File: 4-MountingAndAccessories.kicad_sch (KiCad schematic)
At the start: 16 parts, among them J401 Spring Contact

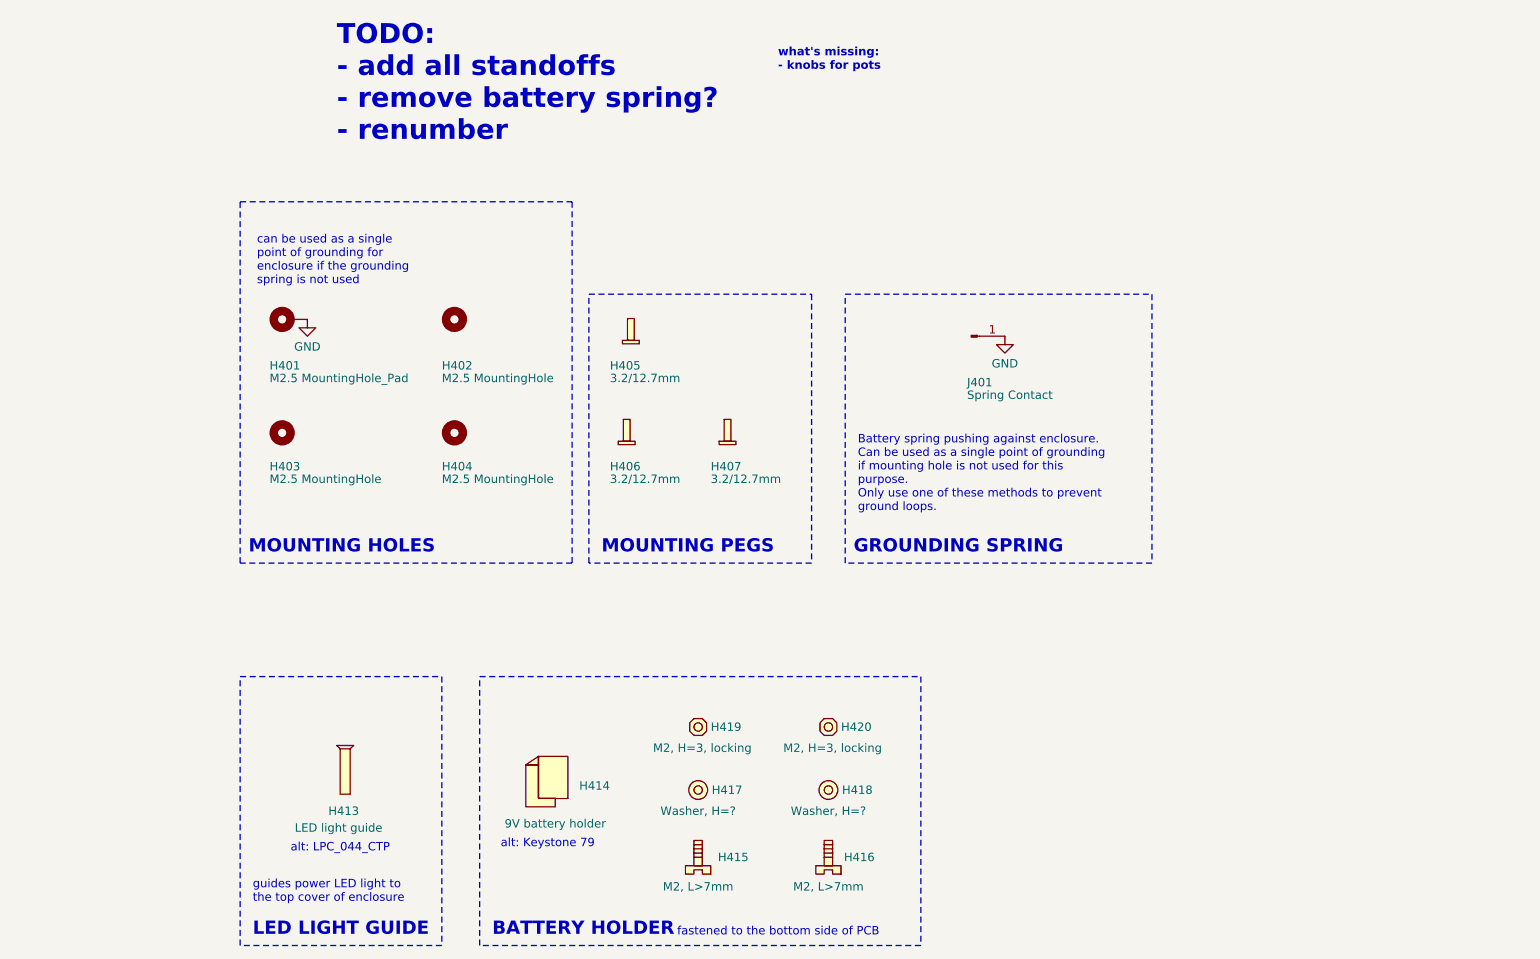
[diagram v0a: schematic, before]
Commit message: schematic: finishing standoffs, screws, minor improvements
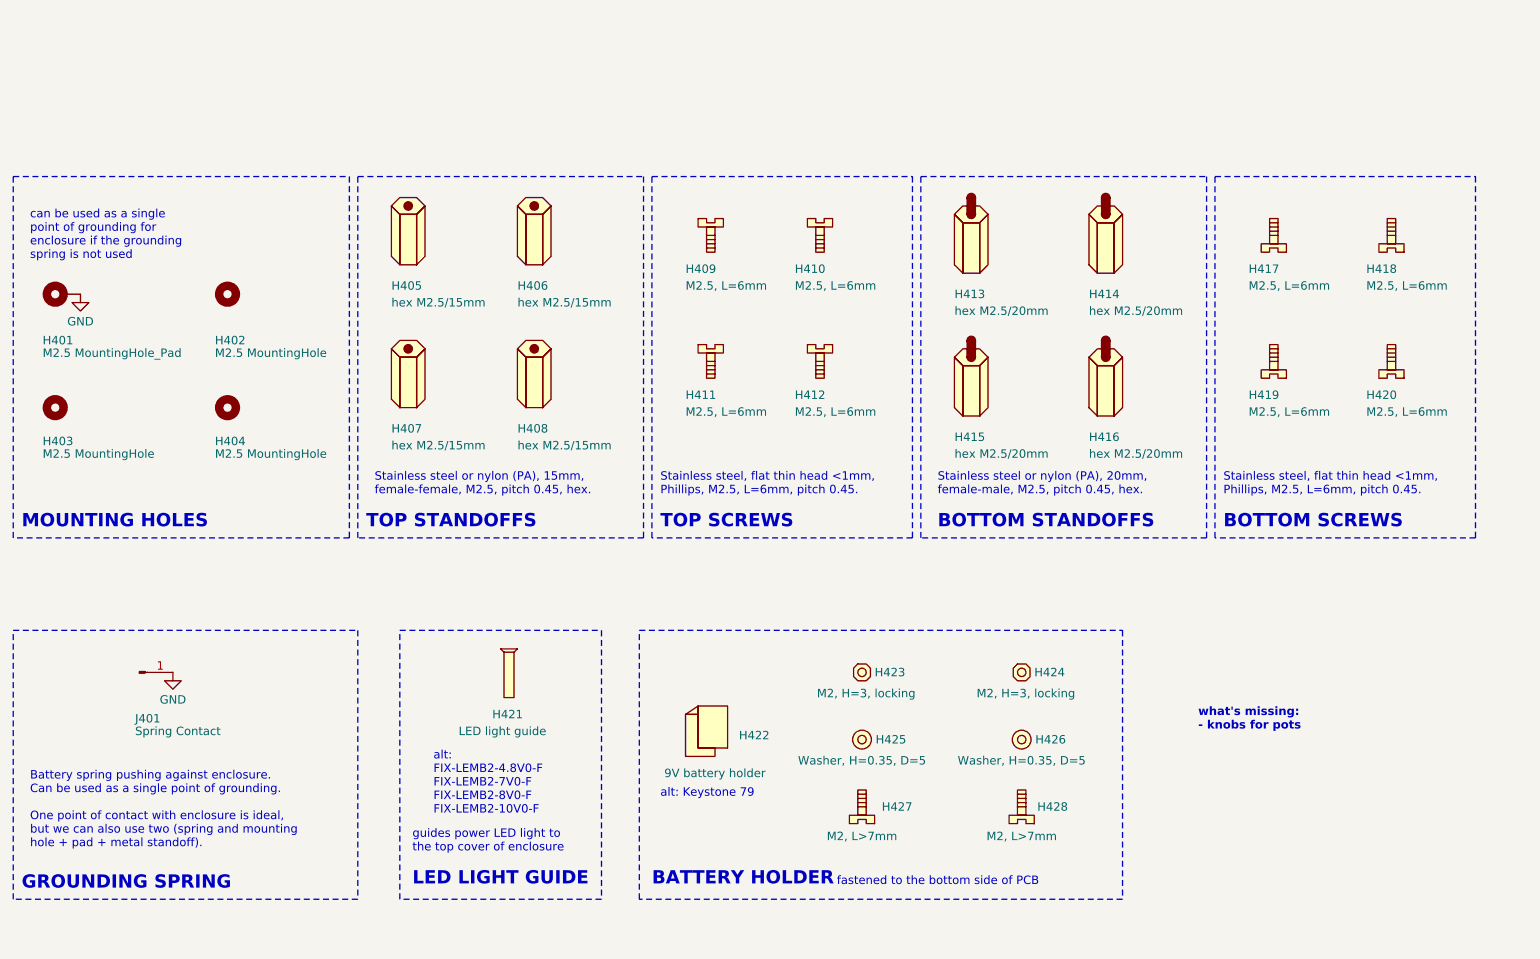
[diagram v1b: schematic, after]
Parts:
- removed H405, H406, H407: 3.2/12.7mm, symbol MountingPegs:MountingPeg
- removed H418: Washer, H=?, symbol Washer:Washer
- added H405, H406, H407, H408: hex M2.5/15mm, symbol StandoffPCB:Standoff_Female_Female
- added H409, H410, H411, H412, H417, H418, H419, H420: M2.5, L=6mm, symbol Bolt:Bolt
- added H413, H414, H415, H416: hex M2.5/20mm, symbol StandoffPCB:Standoff_Female_Male
- added H426: Washer, H=0.35, D=5, symbol Washer:Washer
- H401, H402, H403, H404: now left out of the parts list
- H421: renamed from H413; Mfr Part # PLPC3-10MM -> FIX-LEMB2-10V0-F; Mouser Part # 749-PLPC310MM -> -; Purpose LED light pipe from top of the enclosure to LED -> LED light pipe from top of the enclosure to LED. Dia guide 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; Source Mouser -> TME; TME Part # PLPC3-10MM -> FIX-LEMB2-10V0-F
- H423: renamed from H419; LCSC Part # (none) -> -; Mfr (none) -> -; Mfr Part # (none) -> -; Mouser Part # (none) -> -; TME Part # (none) -> -
- H425: renamed from H417; value Washer, H=? -> Washer, H=0.35, D=5; LCSC Part # (none) -> -; Mfr (none) -> -; Mfr Part # (none) -> -; Mouser Part # (none) -> -; TME Part # (none) -> -
- H427: renamed from H415; LCSC Part # (none) -> -; Mfr (none) -> -; Mfr Part # (none) -> -; Mouser Part # (none) -> -; TME Part # (none) -> -
- H428: renamed from H416; LCSC Part # (none) -> -; Mfr (none) -> -; Mfr Part # (none) -> -; Mouser Part # (none) -> -; Source (none) -> -; TME Part # (none) -> -
- J401: Source TME -> Mouser
- renumbered H414 to H422, H420 to H424
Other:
- note added: "BOTTOM SCREWS"
- note added: "BOTTOM STANDOFFS"
- note added: "Battery spring pushing against enclosure. Can be used as a single point of grounding. One point of contact with enclosure is ideal, but we can also use two (spring and mounting hole + pad + metal standoff)."
- note added: "Stainless steel or nylon (PA), 15mm, female-female, M2.5, pitch 0.45, hex."
- note added: "Stainless steel or nylon (PA), 20mm, female-male, M2.5, pitch 0.45, hex."
- note added: "Stainless steel, flat thin head <1mm, Phillips, M2.5, L=6mm, pitch 0.45."
- note added: "TOP SCREWS"
- note added: "TOP STANDOFFS"
- note added: "alt: FIX-LEMB2-4.8V0-F FIX-LEMB2-7V0-F FIX-LEMB2-8V0-F FIX-LEMB2-10V0-F"
- note removed: "Battery spring pushing against enclosure. Can be used as a single point of grounding if mounting hole is not used for this purpose. Only use one of these methods to prevent ground loops."
- note removed: "MOUNTING PEGS"
- note removed: "TODO: - add all standoffs - remove battery spring? - renumber"
- note removed: "alt: LPC_044_CTP"
- moved on the sheet: H401, H402, H403, H404, H421, H422, H423, H424, H425, H427, H428, J401

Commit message: Schematic, PCB: moving DC ESD protection in front of the switch. Using one 22uF bulk decoupling cap where DC enters the board instead of two 10uF near opamps. Using 22uF instead of 10uF in opamp biasing to remove 10uF from BOM completely
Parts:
- H422: Mfr Part # 71 -> 79; Mouser Part # 534-071 -> 534-079; TME Part # KEYS71 -> KEYS79
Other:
- note added: "alt: Keystone 71 (bit too short)"
- note removed: "alt: Keystone 79"
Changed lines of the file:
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@@
 	(title_block
 		(title "Mounting, hardware and accessories")
-		(date "2024-02-20")
+		(date "2024-03-07")
 		(rev "3.0")
 		(company "Arx")
@@
 		)
 	)
-	(text "alt: Keystone 79"
-		(exclude_from_sim no)
-		(at 139.7 119.38 0)
+	(text "alt: Keystone 71\n(bit too short)"
+		(exclude_from_sim no)
+		(at 139.7 121.92 0)
 		(effects
 			(font
@@
 			)
 		)
-		(property "Datasheet" "https://cz.mouser.com/datasheet/2/215/1-745942.pdf"
+		(property "Datasheet" "https://cz.mouser.com/datasheet/2/215/9-745395.pdf"
 			(at 146.05 108.585 0)
 			(effects
@@
 			)
 		)
-		(property "Mfr Part #" "71"
+		(property "Mfr Part #" "79"
 			(at 146.05 108.585 0)
 			(effects
@@
 			)
 		)
-		(property "Mouser Part #" "534-071"
+		(property "Mouser Part #" "534-079"
 			(at 146.05 108.585 0)
 			(effects
@@
 			)
 		)
-		(property "TME Part #" "KEYS71"
+		(property "TME Part #" "KEYS79"
 			(at 146.05 108.585 0)
 			(effects

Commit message: schematic: optimizing few BOM items (for less costly alternatives), few updates
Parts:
- H421: Alt (none) -> FIX-LEMB2-4.8V0-F, FIX-LEMB2-7V0-F, FIX-LEMB2-8V0-F, FIX-LE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
- H422: Alt (none) -> 71 (too short)
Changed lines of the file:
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@@
 	(title_block
 		(title "Mounting, hardware and accessories")
-		(date "2024-03-07")
+		(date "2024-03-10")
 		(rev "3.0")
 		(company "Arx")
@@
 			)
 		)
+		(property "Alt" "71 (too short)"
+			(at 146.05 108.585 0)
+			(effects
+				(font
+					(size 1.27 1.27)
+				)
+				(hide yes)
+			)
+		)
 		(instances
 			(project "2024_PiezoPreamp3"
@@
 			(at 116.84 100.33 0)
 			(effects
+				(font
+					(size 1.27 1.27)
+				)
+				(hide yes)
+			)
+		)
+		(property "Alt" "FIX-LEMB2-4.8V0-F, FIX-LEMB2-7V0-F, FIX-LEMB2-8V0-F, FIX-LEMB2-10V0-F "
+			(at 116.84 100.33 0)
+			(effects
